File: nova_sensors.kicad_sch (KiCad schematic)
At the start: 93 parts, among them J1 Conn_01x03_Socket, J10 Conn_01x04_Socket, J11 Conn_01x04_Socket, J2 Conn_01x03_Socket, J3 Conn_01x04_Socket, J4 Conn_01x02_Socket, J5 Conn_01x02_Socket, J6 Conn_01x03_Socket, J7 Conn_01x02_Socket, J8 Conn_01x02_Socket, J9 Conn_01x02_Socket, SW1 SW_Push, SW2 SW_DIP_x02, SW3 SW_DIP_x02, U1 AT32F455CET7, U2 MAX3232, U3 MAX13488, U4 MAX13488, U5 LD1117S33TR, U6 XL1509-ADJ, Y1 8Mhz, Y2 32768hz

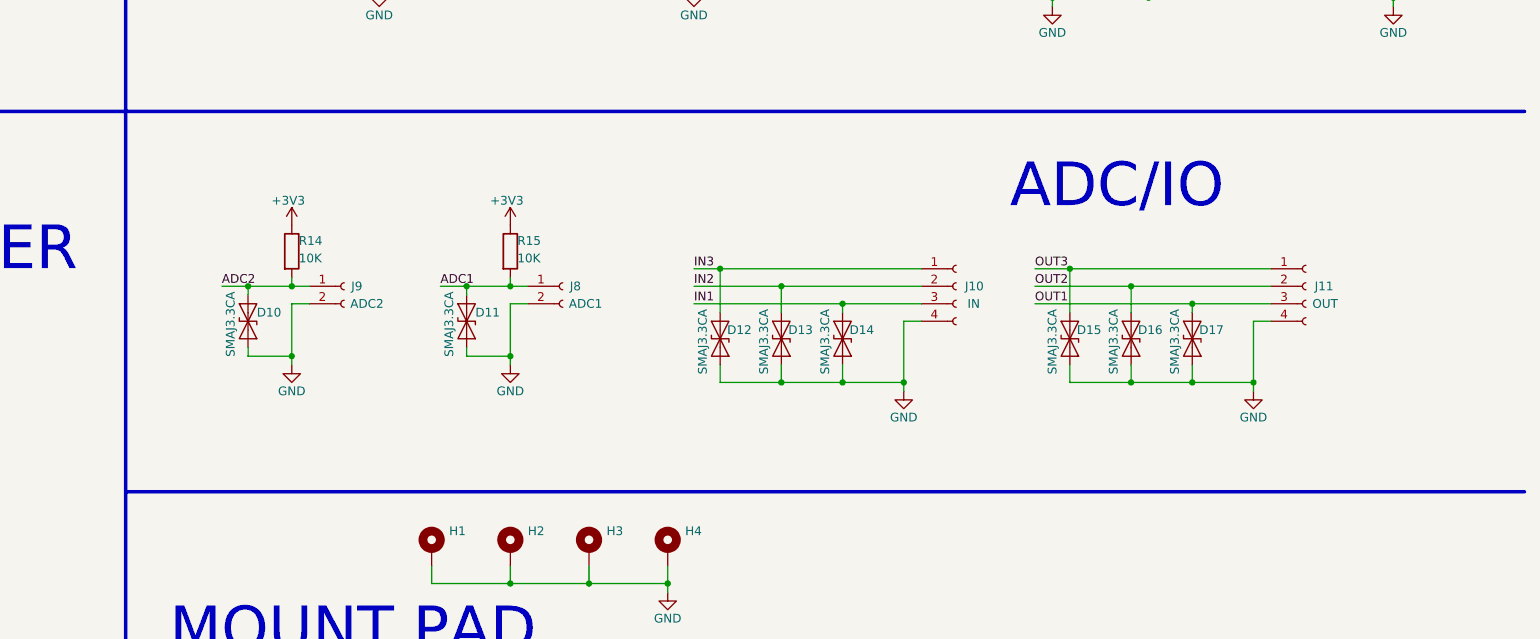
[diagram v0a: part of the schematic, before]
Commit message: fix: 修改ADC电路，将RL分压方向改为接地端；mcu侧增加限流电阻和滤波电容；Rx侧增加滤波电容
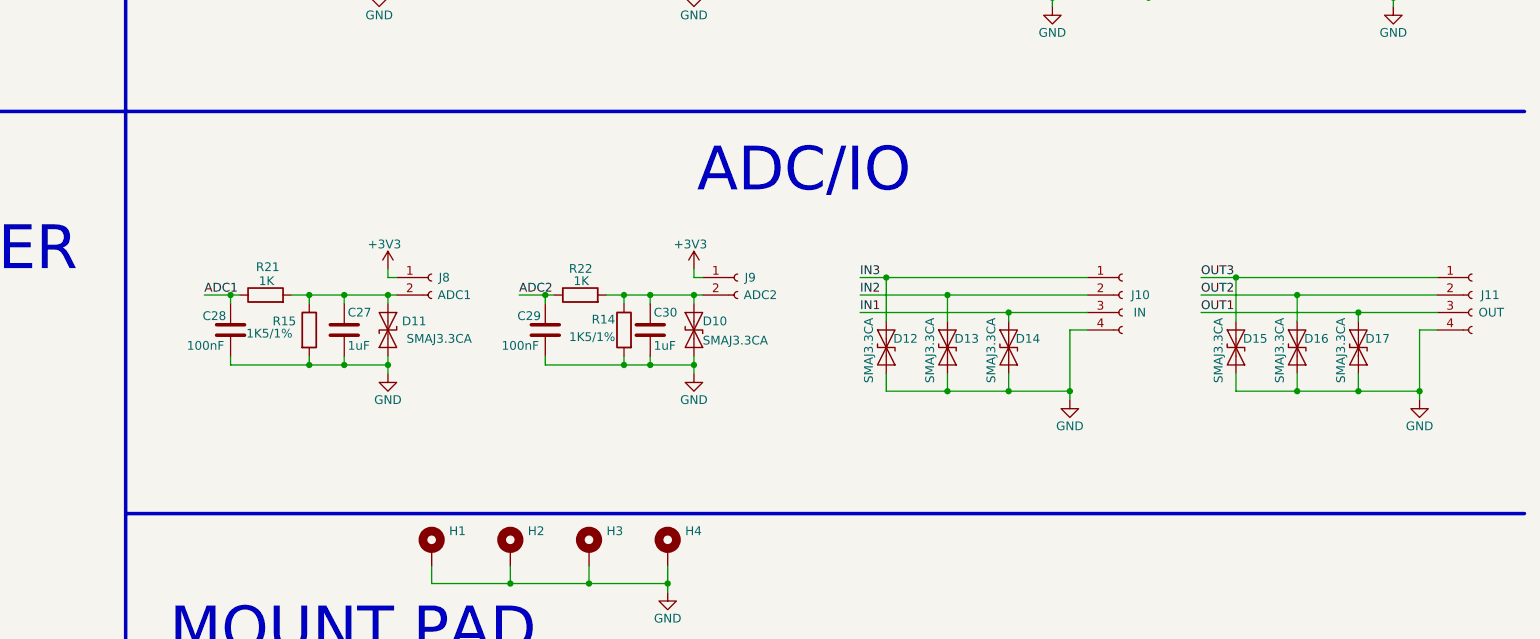
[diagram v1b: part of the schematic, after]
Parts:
- added C27, C30: 1uF, Capacitor_SMD:C_0603_1608Metric, symbol Device:C
- added C28, C29: 100nF, Capacitor_SMD:C_0603_1608Metric, symbol Device:C
- added R21, R22: 1K, Resistor_SMD:R_0603_1608Metric, symbol Device:R
- R14, R15: value 10K -> 1K5/1%
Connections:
- net +3V3: now also J8.1 (Pin_1), J9.1 (Pin_1); no longer R14.1, R15.1
- net ADC1: now also C28.1, R21.1; no longer D11.2 (A2), J8.1 (Pin_1), R15.2
- net ADC2: now also C29.1, R22.1; no longer D10.2 (A2), J9.1 (Pin_1), R14.2
- net GND: now also R14.2, R15.2, C27.2, C28.2, C29.2, C30.2; no longer J8.2 (Pin_2), J9.2 (Pin_2)
- new net: C27.1, D11.2 (A2), J8.2 (Pin_2), R15.1, R21.2
- new net: C30.1, D10.2 (A2), J9.2 (Pin_2), R14.1, R22.2
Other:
- moved on the sheet: D10, D11, D12, D13, D14, D15, D16, D17, J10, J11, J9

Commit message: doc: 修改原理图版本，生成各种生产资料
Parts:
- C12, C9: value 22pF -> 22pF/±1%
- C13, C14: value 12pF -> 12pF/±1%
- C26: value 220uF/16V -> 220uF/35V
- R14, R15: value 1K5/1% -> 1K5/±1%
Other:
- title: 诺瓦控制卡传感器转接板 -> 诺瓦传感器驱动板
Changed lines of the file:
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@@
 	(paper "A3")
 	(title_block
-		(title "诺瓦控制卡传感器转接板")
-		(date "2026-08-31")
-		(rev "V0.0.2")
+		(title "诺瓦传感器驱动板")
+		(date "2026-09-29")
+		(rev "V1.0.0")
 		(company "重庆创迪科技发展有限公司")
 	)
@@
 			)
 		)
-		(property "Value" "12pF"
+		(property "Value" "12pF/±1%"
 			(at 159.893 95.25 90)
 			(show_name no)
@@
 			)
 		)
-		(property "Value" "1K5/1%"
-			(at 221.996 235.458 0)
+		(property "Value" "1K5/±1%"
+			(at 220.472 237.236 0)
 			(show_name no)
 			(do_not_autoplace no)
@@
 			)
 		)
-		(property "Value" "1K5/1%"
-			(at 275.59 235.966 0)
+		(property "Value" "1K5/±1%"
+			(at 275.59 236.982 0)
 			(show_name no)
 			(do_not_autoplace no)
@@
 			)
 		)
-		(property "Value" "220uF/16V"
+		(property "Value" "220uF/35V"
 			(at 154.178 263.144 0)
 			(show_name no)
@@
 			)
 		)
-		(property "Value" "22pF"
+		(property "Value" "22pF/±1%"
 			(at 160.02 73.66 90)
 			(show_name no)
@@
 			)
 		)
-		(property "Value" "12pF"
-			(at 164.973 82.55 90)
+		(property "Value" "12pF/±1%"
+			(at 160.02 82.55 90)
 			(show_name no)
 			(do_not_autoplace no)
@@
 					(size 1.27 1.27)
 				)
-				(justify left)
+				(justify right)
 			)
 		)
@@
 			)
 		)
-		(property "Value" "22pF"
-			(at 164.973 60.96 90)
+		(property "Value" "22pF/±1%"
+			(at 160.02 60.96 90)
 			(show_name no)
 			(do_not_autoplace no)
@@
 					(size 1.27 1.27)
 				)
-				(justify left)
+				(justify right)
 			)
 		)

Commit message: fix: 原理图调整晶振负载电容容值和精度，PCB新增编码丝印
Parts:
- C12, C9: value 22pF/±1% -> 15pF/±5%
- C13, C14: value 12pF/±1% -> 15pF/±5%
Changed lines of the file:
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@@
 			)
 		)
-		(property "Value" "12pF/±1%"
+		(property "Value" "15pF/±5%"
 			(at 159.893 95.25 90)
 			(show_name no)
@@
 			)
 		)
-		(property "Value" "22pF/±1%"
+		(property "Value" "15pF/±5%"
 			(at 160.02 73.66 90)
 			(show_name no)
@@
 			)
 		)
-		(property "Value" "12pF/±1%"
+		(property "Value" "15pF/±5%"
 			(at 160.02 82.55 90)
 			(show_name no)
@@
 			)
 		)
-		(property "Value" "22pF/±1%"
+		(property "Value" "15pF/±5%"
 			(at 160.02 60.96 90)
 			(show_name no)
